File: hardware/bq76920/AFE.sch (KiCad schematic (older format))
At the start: 28 parts, among them Q1 PSMN2R6-40YS, Q2 SI2337DS-T1-E3, Q3 PSMN2R6-40YS, U1 bq76920

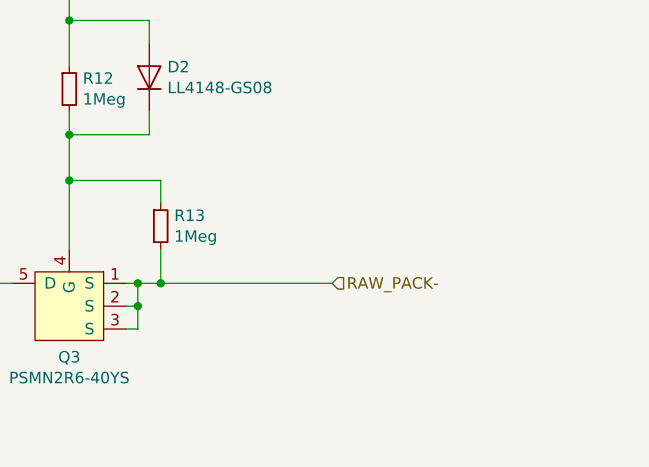
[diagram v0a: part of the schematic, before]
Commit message: remove old project data
Signed-off-by: Ene Alexandru <ene.alexandru@gmail.com>
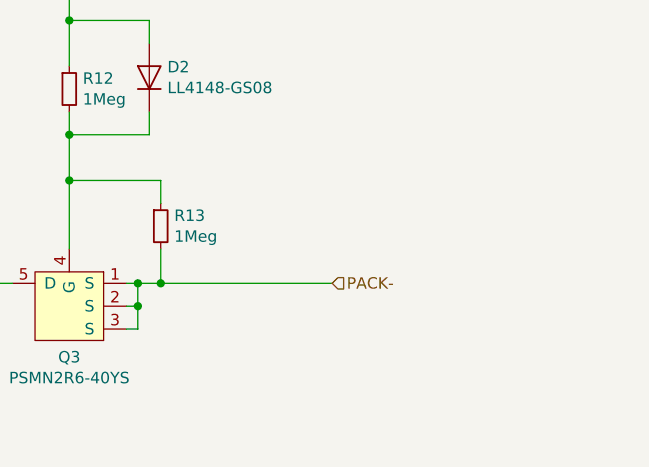
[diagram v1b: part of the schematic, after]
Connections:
- net RAW_PACK- renamed PACK-
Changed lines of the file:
@@
 $Descr A4 11693 8268
 encoding utf-8
-Sheet 2 5
+Sheet 2 4
 Title ""
 Date ""
@@
 Connection ~ 6500 5850
 Text HLabel 7250 5850 2    50   Input ~ 0
-RAW_PACK-
+PACK-
 $Comp
 L Device:Q_PMOS_GSD Q2

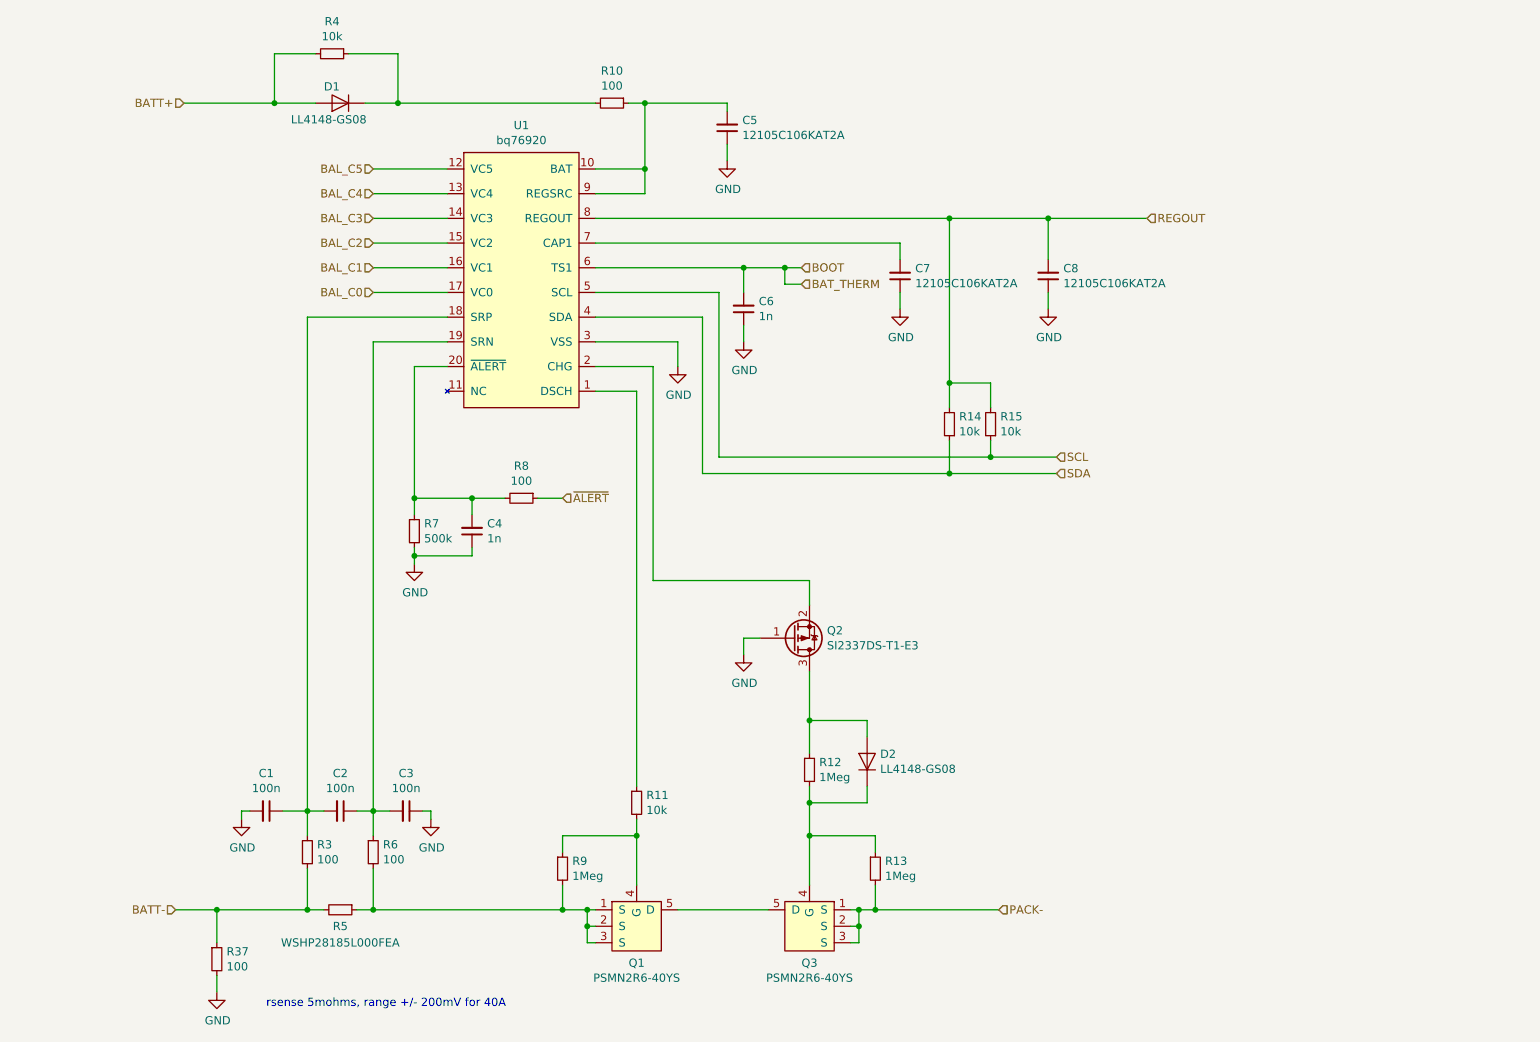
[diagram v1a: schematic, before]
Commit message: update cpu and reduce BOM
Signed-off-by: Ene Alexandru <ene.alexandru@gmail.com>
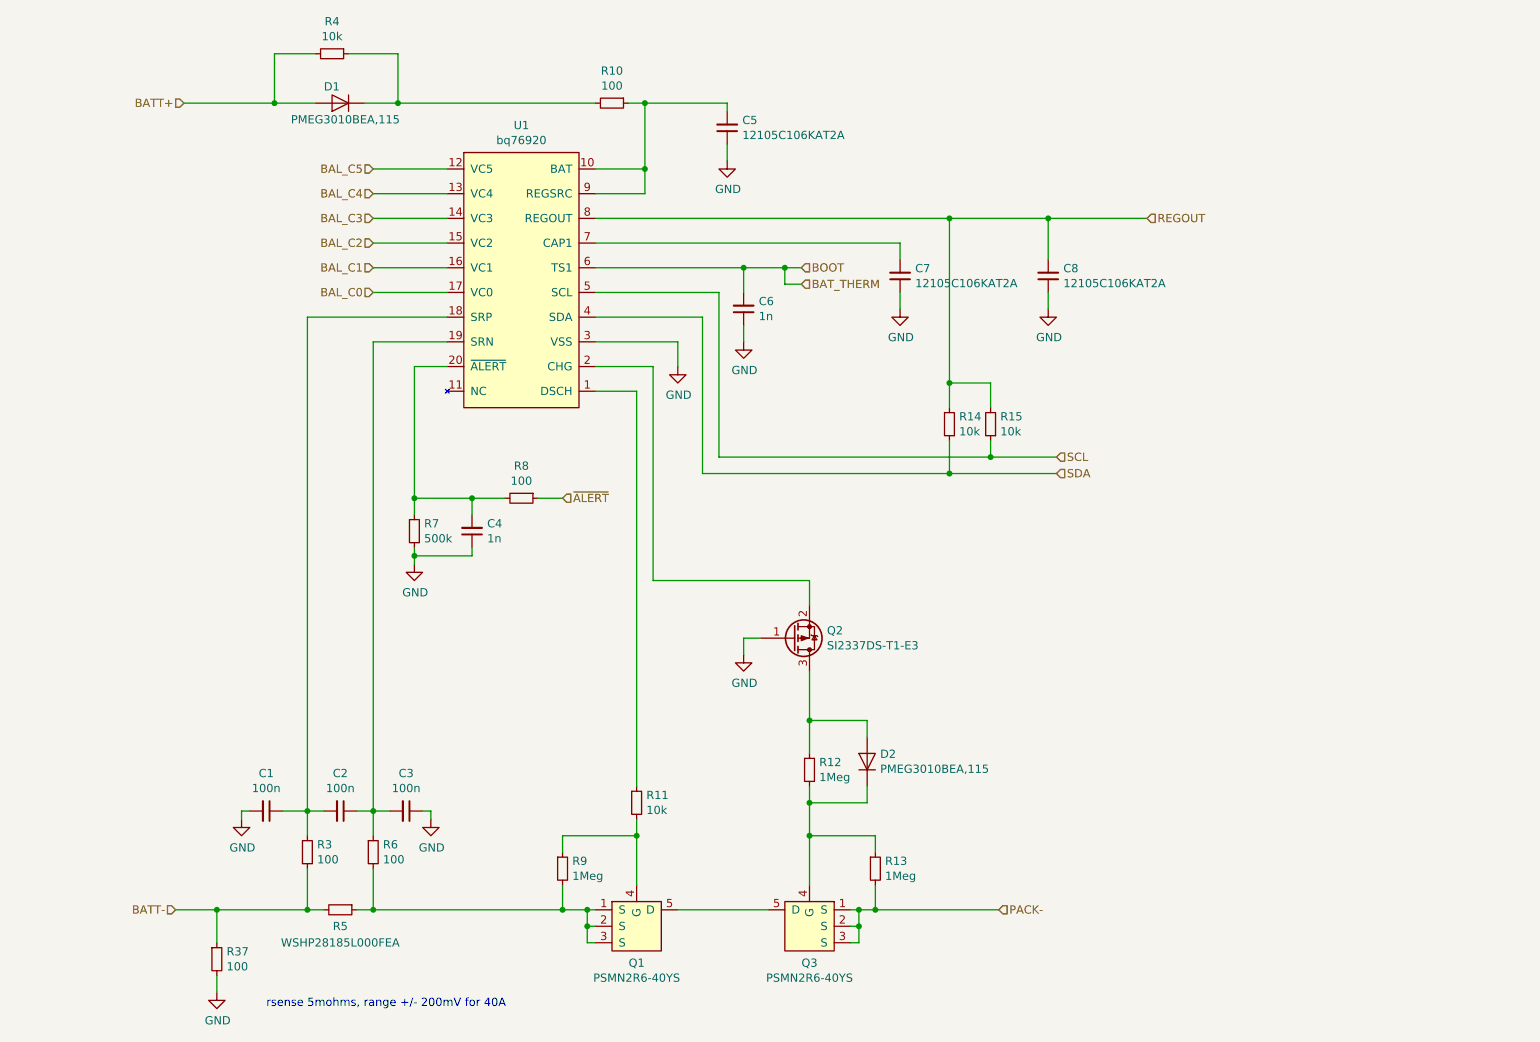
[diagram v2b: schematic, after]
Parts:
- D1, D2: value LL4148-GS08 -> PMEG3010BEA,115; footprint Diode_SMD:D_MiniMELF_Handsoldering -> Diode_SMD:D_SOD-323_HandSoldering
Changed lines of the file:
@@
 P 6450 4950
 F 0 "D2" V 6496 4871 50  0000 R CNN
-F 1 "LL4148-GS08" V 6405 4871 50  0000 R CNN
-F 2 "Diode_SMD:D_MiniMELF_Handsoldering" H 6450 4775 50  0001 C CNN
+F 1 "PMEG3010BEA,115" V 6405 4871 50  0000 R CNN
+F 2 "Diode_SMD:D_SOD-323_HandSoldering" H 6450 4775 50  0001 C CNN
 F 3 "https://assets.nexperia.com/documents/data-sheet/1N4148_1N4448.pdf" H 6450 4950 50  0001 C CNN
 	1    6450 4950
@@
 P 3250 950
 F 0 "D1" H 3350 850 50  0000 R CNN
-F 1 "LL4148-GS08" H 3550 1050 50  0000 R CNN
-F 2 "Diode_SMD:D_MiniMELF_Handsoldering" H 3250 775 50  0001 C CNN
+F 1 "PMEG3010BEA,115" H 3550 1050 50  0000 R CNN
+F 2 "Diode_SMD:D_SOD-323_HandSoldering" H 3250 775 50  0001 C CNN
 F 3 "https://assets.nexperia.com/documents/data-sheet/1N4148_1N4448.pdf" H 3250 950 50  0001 C CNN
 	1    3250 950

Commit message: update bom
Signed-off-by: Ene Alexandru <ene.alexandru@gmail.com>
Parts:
- removed R37: 100, Resistor_SMD:R_0805_2012Metric_Pad1.15x1.40mm_HandSolder, symbol Device:R_Small
- C5, C7, C8: value 12105C106KAT2A -> C1206C475K5RACTU
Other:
- moved on the sheet: C1, C2, C3, C4, C5, C6, C7, C8, D1, D2, Q1, Q2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
